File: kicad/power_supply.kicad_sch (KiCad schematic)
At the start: 23 parts, among them Q1 TIP32, U1 LM78M05_TO220, U2 LM317_TO-220

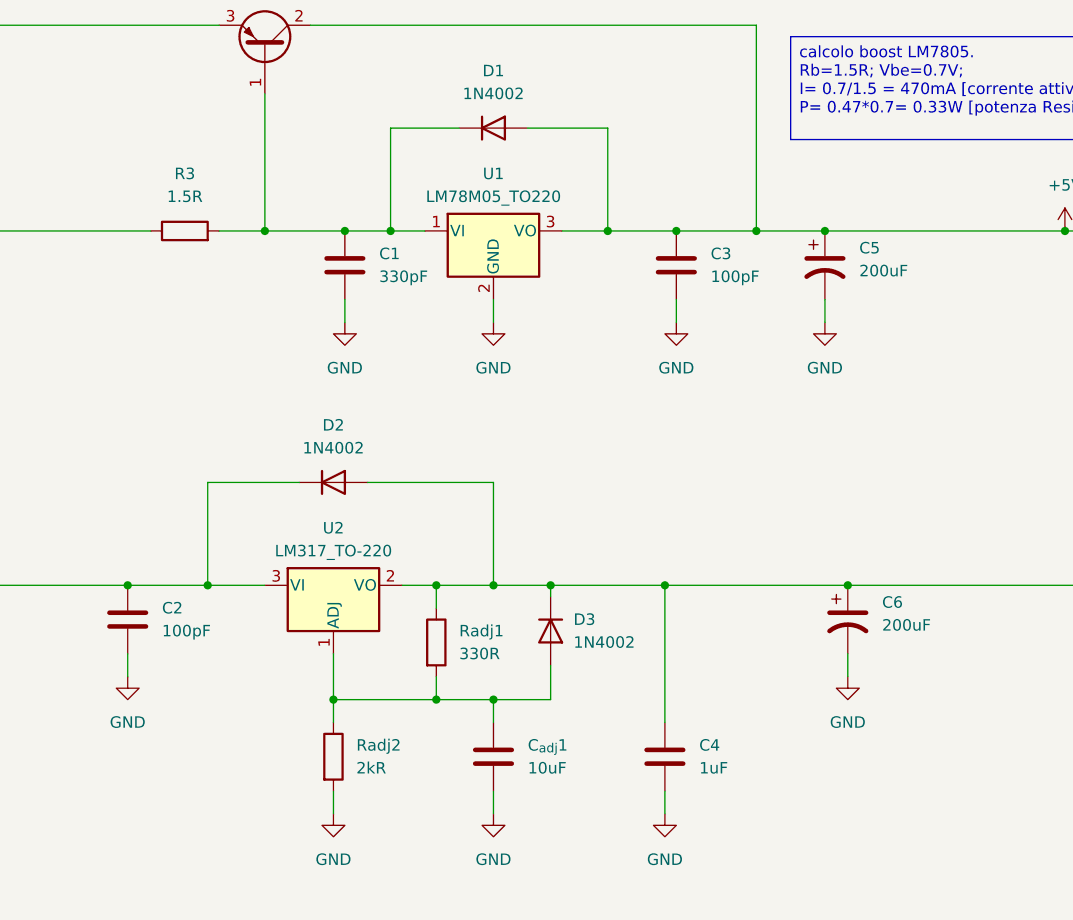
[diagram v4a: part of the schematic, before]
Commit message: terminato collegamento ATMEGA328P
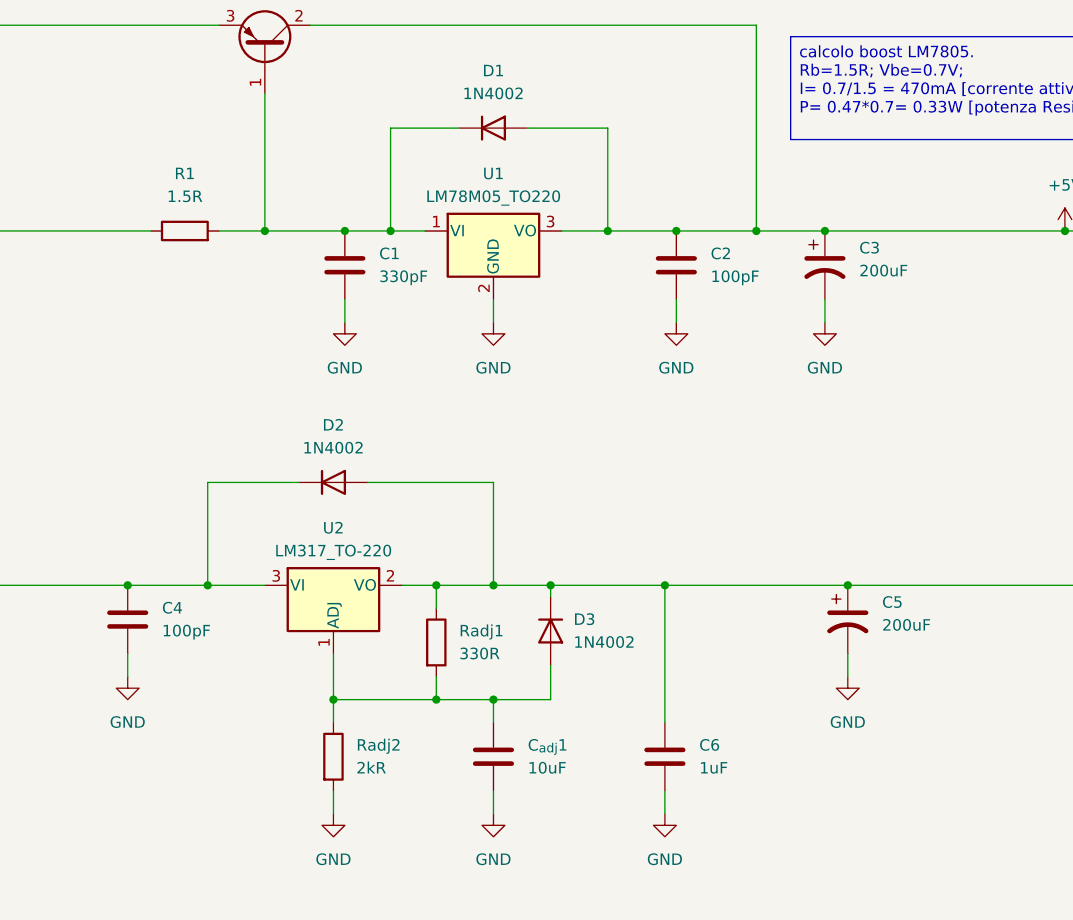
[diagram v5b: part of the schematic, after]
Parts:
- renumbered C3 to C2, C5 to C3, C2 to C4, C6 to C5, C4 to C6, R3 to R1
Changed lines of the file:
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@@
 		(dnp no)
 		(fields_autoplaced yes)
-		(property "Reference" "#PWR012"
+		(property "Reference" "#PWR014"
 			(at 127 165.1 0)
 			(effects
@@
 			(project "electronics-schemas"
 				(path "/f1ade40e-ee4b-4e00-b57d-44850604005b/39ef75b9-0ecd-4ea3-9e5a-3626455f275c"
-					(reference "#PWR012")
+					(reference "#PWR014")
 					(unit 1)
 				)
@@
 		(dnp no)
 		(fields_autoplaced yes)
-		(property "Reference" "#PWR014"
+		(property "Reference" "#PWR013"
 			(at 184.15 149.86 0)
 			(effects
@@
 			(project "electronics-schemas"
 				(path "/f1ade40e-ee4b-4e00-b57d-44850604005b/39ef75b9-0ecd-4ea3-9e5a-3626455f275c"
-					(reference "#PWR014")
+					(reference "#PWR013")
 					(unit 1)
 				)
@@
 		(dnp no)
 		(fields_autoplaced yes)
-		(property "Reference" "#PWR016"
+		(property "Reference" "#PWR06"
 			(at 173.99 59.69 0)
 			(effects
@@
 			(project "electronics-schemas"
 				(path "/f1ade40e-ee4b-4e00-b57d-44850604005b/39ef75b9-0ecd-4ea3-9e5a-3626455f275c"
-					(reference "#PWR016")
+					(reference "#PWR06")
 					(unit 1)
 				)
@@
 		(dnp no)
 		(fields_autoplaced yes)
-		(property "Reference" "#PWR08"
+		(property "Reference" "#PWR09"
 			(at 144.78 110.49 0)
 			(effects
@@
 			(project "electronics-schemas"
 				(path "/f1ade40e-ee4b-4e00-b57d-44850604005b/39ef75b9-0ecd-4ea3-9e5a-3626455f275c"
-					(reference "#PWR08")
+					(reference "#PWR09")
 					(unit 1)
 				)
@@
 		(dnp no)
 		(fields_autoplaced yes)
-		(property "Reference" "#PWR018"
+		(property "Reference" "#PWR07"
 			(at 208.28 97.79 0)
 			(effects
@@
 			(project ""
 				(path "/f1ade40e-ee4b-4e00-b57d-44850604005b/39ef75b9-0ecd-4ea3-9e5a-3626455f275c"
-					(reference "#PWR018")
+					(reference "#PWR07")
 					(unit 1)
 				)
@@
 		(dnp no)
 		(fields_autoplaced yes)
-		(property "Reference" "#PWR09"
+		(property "Reference" "#PWR010"
 			(at 165.1 110.49 0)
 			(effects
@@
 			(project "electronics-schemas"
 				(path "/f1ade40e-ee4b-4e00-b57d-44850604005b/39ef75b9-0ecd-4ea3-9e5a-3626455f275c"
-					(reference "#PWR09")
+					(reference "#PWR010")
 					(unit 1)
 				)
@@
 		(dnp no)
 		(fields_autoplaced yes)
-		(property "Reference" "#PWR019"
+		(property "Reference" "#PWR04"
 			(at 66.04 59.69 0)
 			(effects
@@
 			(project "electronics-schemas"
 				(path "/f1ade40e-ee4b-4e00-b57d-44850604005b/39ef75b9-0ecd-4ea3-9e5a-3626455f275c"
-					(reference "#PWR019")
+					(reference "#PWR04")
 					(unit 1)
 				)
@@
 		(dnp no)
 		(fields_autoplaced yes)
-		(property "Reference" "#PWR010"
+		(property "Reference" "#PWR011"
 			(at 181.61 110.49 0)
 			(effects
@@
 			(project "electronics-schemas"
 				(path "/f1ade40e-ee4b-4e00-b57d-44850604005b/39ef75b9-0ecd-4ea3-9e5a-3626455f275c"
-					(reference "#PWR010")
+					(reference "#PWR011")
 					(unit 1)
 				)
@@
 		(dnp no)
 		(fields_autoplaced yes)
-		(property "Reference" "#PWR04"
+		(property "Reference" "#PWR08"
 			(at 128.27 110.49 0)
 			(effects
@@
 			(project "electronics-schemas"
 				(path "/f1ade40e-ee4b-4e00-b57d-44850604005b/39ef75b9-0ecd-4ea3-9e5a-3626455f275c"
-					(reference "#PWR04")
+					(reference "#PWR08")
 					(unit 1)
 				)
@@
 		(dnp no)
 		(fields_autoplaced yes)
-		(property "Reference" "#PWR017"
+		(property "Reference" "#PWR02"
 			(at 208.28 46.99 0)
 			(effects
@@
 			(project ""
 				(path "/f1ade40e-ee4b-4e00-b57d-44850604005b/39ef75b9-0ecd-4ea3-9e5a-3626455f275c"
-					(reference "#PWR017")
+					(reference "#PWR02")
 					(unit 1)
 				)
@@
 		(dnp no)
 		(fields_autoplaced yes)
-		(property "Reference" "C3"
+		(property "Reference" "C2"
 			(at 168.91 96.5199 0)
 			(effects
@@
 			(project "electronics-schemas"
 				(path "/f1ade40e-ee4b-4e00-b57d-44850604005b/39ef75b9-0ecd-4ea3-9e5a-3626455f275c"
-					(reference "C3")
+					(reference "C2")
 					(unit 1)
 				)
@@
 		(dnp no)
 		(fields_autoplaced yes)
-		(property "Reference" "#PWR02"
+		(property "Reference" "#PWR017"
 			(at 39.37 179.07 0)
 			(effects
@@
 			(project ""
 				(path "/f1ade40e-ee4b-4e00-b57d-44850604005b/39ef75b9-0ecd-4ea3-9e5a-3626455f275c"
-					(reference "#PWR02")
+					(reference "#PWR017")
 					(unit 1)
 				)
@@
 		(dnp no)
 		(fields_autoplaced yes)
-		(property "Reference" "#PWR020"
+		(property "Reference" "#PWR01"
 			(at 39.37 46.99 0)
 			(effects
@@
 			(project ""
 				(path "/f1ade40e-ee4b-4e00-b57d-44850604005b/39ef75b9-0ecd-4ea3-9e5a-3626455f275c"
-					(reference "#PWR020")
+					(reference "#PWR01")
 					(unit 1)
 				)
@@
 		(dnp no)
 		(fields_autoplaced yes)
-		(property "Reference" "#PWR011"
+		(property "Reference" "#PWR012"
 			(at 104.14 149.86 0)
 			(effects
@@
 			(project "electronics-schemas"
 				(path "/f1ade40e-ee4b-4e00-b57d-44850604005b/39ef75b9-0ecd-4ea3-9e5a-3626455f275c"
-					(reference "#PWR011")
+					(reference "#PWR012")
 					(unit 1)
 				)
@@
 		(dnp no)
 		(fields_autoplaced yes)
-		(property "Reference" "#PWR013"
+		(property "Reference" "#PWR016"
 			(at 163.83 165.1 0)
 			(effects
@@
 			(project "electronics-schemas"
 				(path "/f1ade40e-ee4b-4e00-b57d-44850604005b/39ef75b9-0ecd-4ea3-9e5a-3626455f275c"
-					(reference "#PWR013")
+					(reference "#PWR016")
 					(unit 1)
 				)
@@
 		(dnp no)
 		(fields_autoplaced yes)
-		(property "Reference" "#FLG01"
+		(property "Reference" "#FLG02"
 			(at 217.17 41.275 0)
 			(effects
@@
 			(project ""
 				(path "/f1ade40e-ee4b-4e00-b57d-44850604005b/39ef75b9-0ecd-4ea3-9e5a-3626455f275c"
-					(reference "#FLG01")
+					(reference "#FLG02")
 					(unit 1)
 				)
@@
 		(dnp no)
 		(fields_autoplaced yes)
-		(property "Reference" "C5"
+		(property "Reference" "C3"
 			(at 185.42 95.8849 0)
 			(effects
@@
 			(project ""
 				(path "/f1ade40e-ee4b-4e00-b57d-44850604005b/39ef75b9-0ecd-4ea3-9e5a-3626455f275c"
-					(reference "C5")
+					(reference "C3")
 					(unit 1)
 				)
@@
 		(dnp no)
 		(fields_autoplaced yes)
-		(property "Reference" "R3"
+		(property "Reference" "R1"
 			(at 110.49 87.63 90)
 			(effects
@@
 			(project ""
 				(path "/f1ade40e-ee4b-4e00-b57d-44850604005b/39ef75b9-0ecd-4ea3-9e5a-3626455f275c"
-					(reference "R3")
+					(reference "R1")
 					(unit 1)
 				)
@@
 		(dnp no)
 		(fields_autoplaced yes)
-		(property "Reference" "#PWR015"
+		(property "Reference" "#PWR05"
 			(at 161.29 59.69 0)
 			(effects
@@
 			(project "electronics-schemas"
 				(path "/f1ade40e-ee4b-4e00-b57d-44850604005b/39ef75b9-0ecd-4ea3-9e5a-3626455f275c"
-					(reference "#PWR015")
+					(reference "#PWR05")
 					(unit 1)
 				)
@@
 		(dnp no)
 		(fields_autoplaced yes)
-		(property "Reference" "#FLG02"
+		(property "Reference" "#FLG01"
 			(at 29.21 41.275 0)
 			(effects
@@
 			(project ""
 				(path "/f1ade40e-ee4b-4e00-b57d-44850604005b/39ef75b9-0ecd-4ea3-9e5a-3626455f275c"
-					(reference "#FLG02")
+					(reference "#FLG01")
 					(unit 1)
 				)
@@
 		(dnp no)
 		(fields_autoplaced yes)
-		(property "Reference" "C2"
+		(property "Reference" "C4"
 			(at 107.95 135.8899 0)
 			(effects
@@
 			(project "electronics-schemas"
 				(path "/f1ade40e-ee4b-4e00-b57d-44850604005b/39ef75b9-0ecd-4ea3-9e5a-3626455f275c"
-					(reference "C2")
+					(reference "C4")
 					(unit 1)
 				)
@@
 		(dnp no)
 		(fields_autoplaced yes)
-		(property "Reference" "C4"
+		(property "Reference" "C6"
 			(at 167.64 151.1299 0)
 			(effects
@@
 			(project "electronics-schemas"
 				(path "/f1ade40e-ee4b-4e00-b57d-44850604005b/39ef75b9-0ecd-4ea3-9e5a-3626455f275c"
-					(reference "C4")
+					(reference "C6")
 					(unit 1)
 				)
@@
 		(dnp no)
 		(fields_autoplaced yes)
-		(property "Reference" "#PWR021"
+		(property "Reference" "#PWR015"
 			(at 144.78 165.1 0)
 			(effects
@@
 			(project "electronics-schemas"
 				(path "/f1ade40e-ee4b-4e00-b57d-44850604005b/39ef75b9-0ecd-4ea3-9e5a-3626455f275c"
-					(reference "#PWR021")
+					(reference "#PWR015")
 					(unit 1)
 				)
@@
 		(dnp no)
 		(fields_autoplaced yes)
-		(property "Reference" "C6"
+		(property "Reference" "C5"
 			(at 187.96 135.2549 0)
 			(effects
@@
 			(project "electronics-schemas"
 				(path "/f1ade40e-ee4b-4e00-b57d-44850604005b/39ef75b9-0ecd-4ea3-9e5a-3626455f275c"
-					(reference "C6")
-					(unit 1)
-				)
+					(reference "C5")
+					(unit 1)
+				)
